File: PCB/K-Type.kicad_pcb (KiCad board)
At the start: 2 copper layers, 357.5 x 131.8 mm, 362 parts, among them J1 USBC, J2 USBC, P1 FLASH_HDR, P2 CONN_16, U1 MK20DX256VLH7, U2 TS3DS10224, U3 TS3USB30E, U4 IS31FL3733, U5 IS31FL3733, X1 CRYSTAL

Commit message: Adding final cross traces
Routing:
- net /ledmatrix/LD2_CS4: track 22.7 -> 384.0 mm, vias 4 -> 24
- net /ledmatrix/LD2_CS3: track 47.2 -> 360.1 mm, vias 6 -> 28
- net /ledmatrix/LD2_CS2: track 71.7 -> 340.5 mm, vias 8 -> 29
- net /ledmatrix/LD2_CS1: track 95.8 -> 315.2 mm, vias 12 -> 28
- net /ledmatrix/LD2_CS15: track 202.8 -> 301.4 mm, vias 12 -> 21

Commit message: add more traces
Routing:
- net /ledmatrix/LD1_CS2: track 87.2 -> 452.9 mm, vias 4 -> 38
- net /ledmatrix/LD1_CS1: track 70.1 -> 428.3 mm, vias 6 -> 31
- net /ledmatrix/LD2_CS13: track 125.0 -> 469.4 mm, vias 10 -> 36
- net /ledmatrix/LD2_CS10: track 31.0 -> 344.5 mm, vias 4 -> 42
- net /ledmatrix/LD2_CS9: track 66.4 -> 378.6 mm, vias 8 -> 43
- net /ledmatrix/LD1_CS16: track 75.7 -> 352.7 mm, vias 8 -> 20
- net /ledmatrix/LD2_CS11: track 58.7 -> 305.8 mm, vias 4 -> 37
- net /ledmatrix/LD2_CS8: track 110.4 -> 348.4 mm, vias 6 -> 31
- net /ledmatrix/LD2_CS12: track 74.4 -> 306.7 mm, vias 8 -> 38
- net /ledmatrix/LD2_CS7: track 132.7 -> 351.5 mm, vias 6 -> 17
- net /ledmatrix/LD2_CS6: track 154.4 -> 321.0 mm, vias 6 -> 19
- net /ledmatrix/LD2_CS14: track 158.3 -> 306.1 mm, vias 10 -> 11
- net /ledmatrix/LD2_CS5: track 175.4 -> 311.1 mm, vias 6 -> 12
- net /ledmatrix/LD1_CS3: track 269.7 -> 381.4 mm, vias 4 -> 14
- net /ledmatrix/LD1_CS6: track 218.4 -> 327.0 mm, vias 8 -> 21
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
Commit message: Added some more traces
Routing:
- net /mcu/SHLD: track 60.7 -> 254.5 mm, vias 3 -> 4
- net /ledmatrix/LD2_CS14: track 306.1 -> 471.8 mm, vias 11 -> 18
- net /ledmatrix/LD1_CS9: track 161.8 -> 304.9 mm, vias 6 -> 15
- net /ledmatrix/LD1_CS10: track 138.2 -> 272.7 mm, vias 6 -> 13
- net /ledmatrix/LD2_CS12: track 306.7 -> 384.7 mm, vias 38 -> 39
- net /ledmatrix/LD1_CS11: track 124.3 -> 195.8 mm, vias 6 -> 11
- net /ledmatrix/LD1_CS12: track 103.4 -> 165.1 mm, vias 6 -> 10
- net /ledmatrix/LD1_CS14: track 72.3 -> 101.6 mm, vias 6 -> 7
- net /ledmatrix/LD1_CS13: track 89.0 -> 117.7 mm, vias 6 -> 7
- net /ledmatrix/LD2_CS7: track 351.5 -> 370.3 mm, vias 17 -> 19

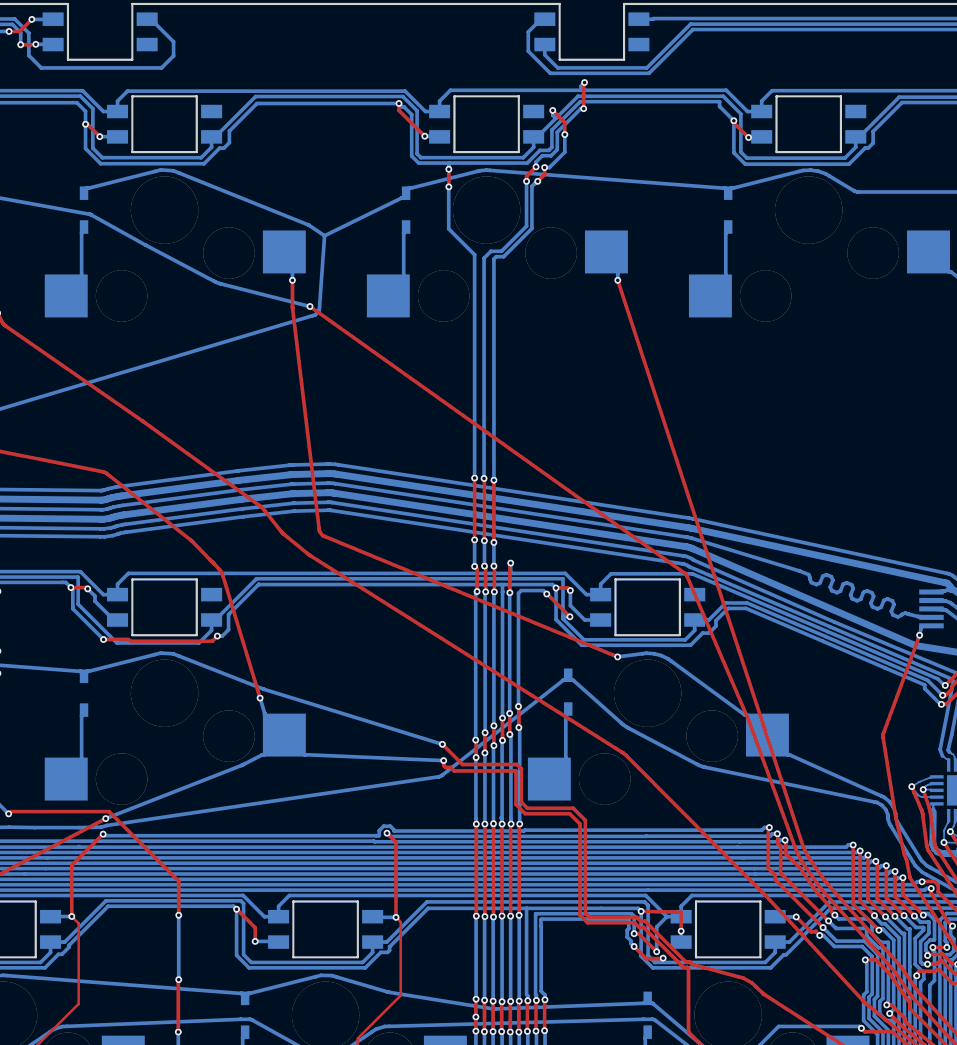
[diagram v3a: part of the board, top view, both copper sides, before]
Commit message: Added some more traces
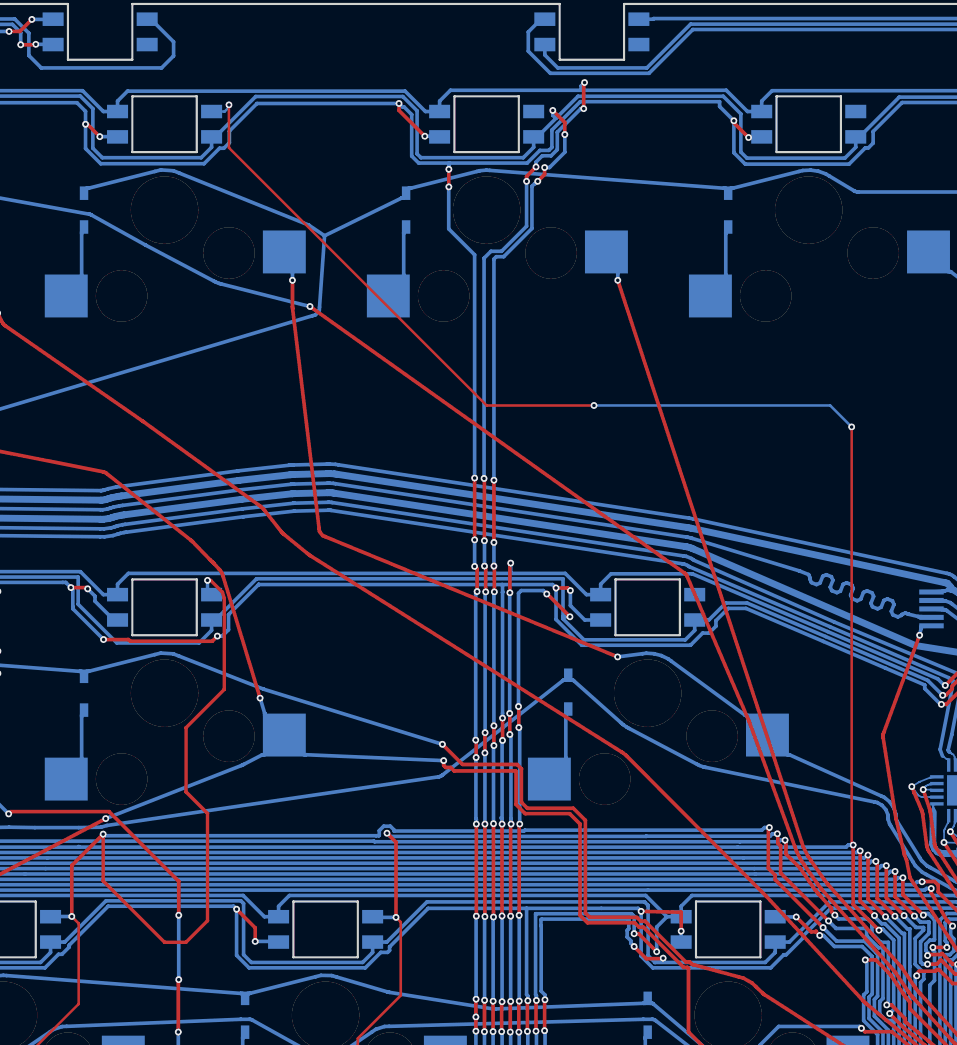
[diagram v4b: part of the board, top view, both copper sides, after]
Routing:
- net /ledmatrix/LD1_CS11: track 195.8 -> 268.1 mm, vias 11 -> 14
- net /ledmatrix/LD1_CS13: track 117.7 -> 151.7 mm, vias 7 -> 8
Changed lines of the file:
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@@
     (thickness 1.6002)
     (drawings 1427)
-    (tracks 21540)
+    (tracks 21568)
     (zones 0)
     (modules 362)
@@
   )
   (setup
-    (last_trace_width 0.1524)
+    (last_trace_width 0.2032)
     (user_trace_width 0.1016)
     (user_trace_width 0.1524)
@@
   (segment (start 235.585 65.8495) (end 239.395 69.6595) (width 0.1524) (layer Front) (net 179))
   (segment (start 239.395 69.6595) (end 239.395 74.7395) (width 0.1524) (layer Front) (net 179))
+  (segment (start 273.431 37.0325) (end 273.685 36.7785) (width 0.1524) (layer Back) (net 179))
+  (segment (start 272.6563 37.0325) (end 273.431 37.0325) (width 0.1524) (layer Back) (net 179))
+  (via (at 273.685 36.6395) (size 0.4064) (drill 0.2032) (layers Front Back) (net 179))
+  (segment (start 273.685 36.7785) (end 273.685 36.6395) (width 0.1524) (layer Back) (net 179))
+  (segment (start 273.685 39.1795) (end 288.925 54.4195) (width 0.1524) (layer Front) (net 179))
+  (segment (start 273.685 36.6395) (end 273.685 39.1795) (width 0.1524) (layer Front) (net 179))
+  (via (at 295.275 54.4195) (size 0.4064) (drill 0.2032) (layers Front Back) (net 179))
+  (segment (start 288.925 54.4195) (end 295.275 54.4195) (width 0.1524) (layer Front) (net 179))
+  (segment (start 295.275 54.4195) (end 309.245 54.4195) (width 0.1524) (layer Back) (net 179))
+  (via (at 310.515 55.6895) (size 0.4064) (drill 0.2032) (layers Front Back) (net 179))
+  (segment (start 309.245 54.4195) (end 310.515 55.6895) (width 0.1524) (layer Back) (net 179))
+  (segment (start 310.515 80.327834) (end 310.603733 80.416567) (width 0.1524) (layer Front) (net 179))
+  (segment (start 310.515 55.6895) (end 310.515 80.327834) (width 0.1524) (layer Front) (net 179))
   (segment (start 322.5341 106.4108) (end 323.0651 105.8403) (width 0.1016) (layer Back) (net 180))
   (segment (start 322.4174 106.5599) (end 322.3874 106.6156) (width 0.1016) (layer Back) (net 180))
@@
   (segment (start 264.795 85.0519) (end 264.3886 84.6455) (width 0.1524) (layer Front) (net 181))
   (segment (start 264.795 89.817258) (end 264.795 85.0519) (width 0.1524) (layer Front) (net 181))
+  (segment (start 266.2428 79.773294) (end 266.2428 82.5373) (width 0.2032) (layer Front) (net 181))
+  (segment (start 266.2428 82.5373) (end 269.875 86.1695) (width 0.2032) (layer Front) (net 181))
+  (segment (start 269.875 86.1695) (end 271.145 86.1695) (width 0.2032) (layer Front) (net 181))
+  (segment (start 271.145 86.1695) (end 272.415 84.8995) (width 0.2032) (layer Front) (net 181))
+  (segment (start 272.415 84.8995) (end 272.415 78.5495) (width 0.2032) (layer Front) (net 181))
+  (segment (start 272.415 78.5495) (end 271.145 77.2795) (width 0.2032) (layer Front) (net 181))
+  (segment (start 273.405601 65.819422) (end 273.296696 65.461196) (width 0.2032) (layer Front) (net 181))
+  (segment (start 273.405601 71.215015) (end 273.405601 65.819422) (width 0.2032) (layer Front) (net 181))
+  (segment (start 271.145 77.2795) (end 271.145 73.475616) (width 0.2032) (layer Front) (net 181))
+  (segment (start 271.145 73.475616) (end 273.405601 71.215015) (width 0.2032) (layer Front) (net 181))
+  (via (at 272.415 64.7637) (size 0.4064) (drill 0.2032) (layers Front Back) (net 181))
+  (segment (start 273.296696 65.461196) (end 272.5992 64.7637) (width 0.2032) (layer Front) (net 181))
+  (segment (start 272.5992 64.7637) (end 272.415 64.7637) (width 0.2032) (layer Front) (net 181))
+  (segment (start 272.415 65.3662) (end 272.6563 65.6075) (width 0.2032) (layer Back) (net 181))
+  (segment (start 272.415 64.7637) (end 272.415 65.3662) (width 0.2032) (layer Back) (net 181))
   (segment (start 322.9398 108.0113) (end 323.3776 107.7038) (width 0.1016) (layer Back) (net 182))
   (segment (start 322.8503 108.0742) (end 322.9398 108.0113) (width 0.1016) (layer Back) (net 182))
